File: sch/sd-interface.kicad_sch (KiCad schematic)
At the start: 33 parts, among them J15 F32Q-1A7H1-11022, J16 MEM2075-00-140-01-A, J17 5V_out, J19 3V3_in, Q1 Q_PMOS_GSD, U10 CD4043BDR, U11 TPS22919DCKR, U8 MAX4996LETG_

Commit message: started pcb design
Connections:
- net R_En_switch: now also U10.3 (R1)
- net S_En_switch: now also U10.4 (S1)
- net at TP19.1, U10.10 (Q3), U8.15 (EN): no longer R15.2, R16.1
- net at U10.2 (Q1): now also R15.2, R16.1
- no-connect marks 7 -> 4
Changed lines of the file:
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@@
+	)
+	(junction
+		(at 302.26 132.08)
+		(diameter 0)
+		(color 0 0 0 0)
 	)
 	(junction
@@
 	)
 	(junction
-		(at 204.47 144.78)
+		(at 302.26 142.24)
 		(diameter 0)
 		(color 0 0 0 0)
@@
 	)
 	(no_connect
-		(at 299.72 147.32)
-	)
-	(no_connect
 		(at 299.72 125.73)
 	)
@@
 	)
 	(no_connect
-		(at 299.72 137.16)
-	)
-	(no_connect
 		(at 279.4 227.33)
 	)
@@
 		(at 175.26 266.7)
 	)
-	(no_connect
-		(at 264.16 149.86)
-	)
 	(wire
 		(pts
@@
 	(wire
 		(pts
+			(xy 299.72 137.16) (xy 302.26 137.16)
+		)
+		(stroke
+			(width 0)
+			(type default)
+		)
+	)
+	(wire
+		(pts
 			(xy 152.4 66.04) (xy 152.4 69.85)
 		)
@@
 	(wire
 		(pts
-			(xy 204.47 151.13) (xy 204.47 144.78)
-		)
-		(stroke
-			(width 0)
-			(type default)
-		)
-	)
-	(wire
-		(pts
 			(xy 234.95 73.66) (xy 234.95 62.23)
 		)
@@
 	(wire
 		(pts
+			(xy 302.26 132.08) (xy 335.28 132.08)
+		)
+		(stroke
+			(width 0)
+			(type default)
+		)
+	)
+	(wire
+		(pts
 			(xy 99.06 163.83) (xy 99.06 190.5)
 		)
@@
 	(wire
 		(pts
-			(xy 299.72 142.24) (xy 335.28 142.24)
+			(xy 299.72 142.24) (xy 302.26 142.24)
 		)
 		(stroke
@@
 	(wire
 		(pts
+			(xy 215.9 149.86) (xy 215.9 229.87)
+		)
+		(stroke
+			(width 0)
+			(type default)
+		)
+	)
+	(wire
+		(pts
 			(xy 71.12 87.63) (xy 71.12 123.19)
 		)
@@
 	(wire
 		(pts
-			(xy 215.9 151.13) (xy 204.47 151.13)
-		)
-		(stroke
-			(width 0)
-			(type default)
-		)
-	)
-	(wire
-		(pts
 			(xy 346.71 218.44) (xy 346.71 220.98)
 		)
@@
 	(wire
 		(pts
-			(xy 215.9 229.87) (xy 215.9 151.13)
-		)
-		(stroke
-			(width 0)
-			(type default)
-		)
-	)
-	(wire
-		(pts
 			(xy 111.76 36.83) (xy 111.76 50.8)
 		)
@@
 	(wire
 		(pts
+			(xy 302.26 142.24) (xy 335.28 142.24)
+		)
+		(stroke
+			(width 0)
+			(type default)
+		)
+	)
+	(wire
+		(pts
+			(xy 264.16 149.86) (xy 215.9 149.86)
+		)
+		(stroke
+			(width 0)
+			(type default)
+		)
+	)
+	(wire
+		(pts
 			(xy 207.01 62.23) (xy 234.95 62.23)
 		)
@@
 	(wire
 		(pts
+			(xy 302.26 142.24) (xy 302.26 147.32)
+		)
+		(stroke
+			(width 0)
+			(type default)
+		)
+	)
+	(wire
+		(pts
 			(xy 96.52 36.83) (xy 99.06 36.83)
 		)
@@
 	(wire
 		(pts
-			(xy 299.72 132.08) (xy 335.28 132.08)
+			(xy 299.72 132.08) (xy 302.26 132.08)
 		)
 		(stroke
@@
 	(wire
 		(pts
+			(xy 302.26 137.16) (xy 302.26 132.08)
+		)
+		(stroke
+			(width 0)
+			(type default)
+		)
+	)
+	(wire
+		(pts
 			(xy 130.81 203.2) (xy 173.99 203.2)
 		)
@@
 		)
 		(stroke
+			(width 0)
+			(type default)
+		)
+	)
+	(wire
+		(pts
+			(xy 302.26 147.32) (xy 299.72 147.32)
+		)
+		(stroke

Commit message: work pcb about 70 percent
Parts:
- TP10, TP11, TP12, TP7, TP8, TP9: footprint TestPoint:TestPoint_Loop_D2.50mm_Drill1.85mm -> TestPoint:TestPoint_Pad_D1.0mm
- TP13, TP14, TP15, TP16, TP17, TP18, TP19: footprint TestPoint:TestPoint_Loop_D2.50mm_Drill1.85mm -> TestPoint:TestPoint_Loop_D2.60mm_Drill1.6mm_Beaded
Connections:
- net +3V3_e is gone; now on net +3V3: C20.1, C9.1, J19.1, Q1.2 (S), R15.1, U8.14 (VCC)
- net +3v3_e is gone; now on net +3V3: C13.1, U10.16 (VDD), U10.5 (EN)
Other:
- note removed: "CIRCUIT IS DESIGNED FOR ONLY 3.3V SD OPERATION, NOT 1.8V"
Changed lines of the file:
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@@
 		)
 	)
-	(text "CIRCUIT IS DESIGNED FOR ONLY 3.3V SD \nOPERATION, NOT 1.8V"
-		(exclude_from_sim no)
-		(at 304.8 29.718 0)
-		(effects
-			(font
-				(size 1.27 1.27)
-			)
-		)
-	)
 	(text "8: DAT1 // X"
 		(exclude_from_sim no)
@@
 		)
 	)
-	(global_label "+3V3_e"
+	(global_label "+3V3"
 		(shape input)
 		(at 146.05 153.67 0)
@@
 		)
 		(property "Intersheetrefs" "${INTERSHEET_REFS}"
-			(at 156.1714 153.67 0)
+			(at 154.1152 153.67 0)
 			(effects
 				(font
@@
 		)
 	)
-	(global_label "+3V3_e"
+	(global_label "+3V3"
 		(shape input)
 		(at 194.31 222.25 180)
@@
 		)
 	)
-	(global_label "+3v3_e"
+	(global_label "+3V3"
 		(shape input)
 		(at 252.73 154.94 180)
@@
 		)
 		(property "Intersheetrefs" "${INTERSHEET_REFS}"
-			(at 246.3582 154.94 0)
+			(at 244.6648 154.94 0)
 			(effects
 				(font
@@
 		)
 	)
-	(global_label "+3V3_e"
+	(global_label "+3V3"
 		(shape output)
 		(at 313.69 48.26 180)
@@
 		)
 		(property "Intersheetrefs" "${INTERSHEET_REFS}"
-			(at 303.5686 48.26 0)
+			(at 305.6248 48.26 0)
 			(effects
 				(font
@@
 			)
 		)
-		(property "Footprint" "TestPoint:TestPoint_Loop_D2.50mm_Drill1.85mm"
+		(property "Footprint" "TestPoint:TestPoint_Loop_D2.60mm_Drill1.6mm_Beaded"
 			(at 213.36 73.66 0)
 			(effects
@@
 			)
 		)
-		(property "Footprint" "TestPoint:TestPoint_Loop_D2.50mm_Drill1.85mm"
+		(property "Footprint" "TestPoint:TestPoint_Loop_D2.60mm_Drill1.6mm_Beaded"
 			(at 200.66 261.62 0)
 			(effects
@@
 			)
 		)
-		(property "Footprint" "TestPoint:TestPoint_Loop_D2.50mm_Drill1.85mm"
+		(property "Footprint" "TestPoint:TestPoint_Pad_D1.0mm"
 			(at 76.2 158.75 0)
 			(effects
@@
 			)
 		)
-		(property "Footprint" "TestPoint:TestPoint_Loop_D2.50mm_Drill1.85mm"
+		(property "Footprint" "TestPoint:TestPoint_Loop_D2.60mm_Drill1.6mm_Beaded"
 			(at 222.25 73.66 0)
 			(effects
@@
 			)
 		)
-		(property "Footprint" "TestPoint:TestPoint_Loop_D2.50mm_Drill1.85mm"
+		(property "Footprint" "TestPoint:TestPoint_Loop_D2.60mm_Drill1.6mm_Beaded"
 			(at 252.73 138.43 0)
 			(effects
@@
 			)
 		)
-		(property "Footprint" "TestPoint:TestPoint_Loop_D2.50mm_Drill1.85mm"
+		(property "Footprint" "TestPoint:TestPoint_Pad_D1.0mm"
 			(at 91.44 158.75 0)
 			(effects
@@
 			)
 		)
-		(property "Footprint" "TestPoint:TestPoint_Loop_D2.50mm_Drill1.85mm"
+		(property "Footprint" "TestPoint:TestPoint_Loop_D2.60mm_Drill1.6mm_Beaded"
 			(at 229.87 73.66 0)
 			(effects
@@
 			)
 		)
-		(property "Footprint" "TestPoint:TestPoint_Loop_D2.50mm_Drill1.85mm"
+		(property "Footprint" "TestPoint:TestPoint_Loop_D2.60mm_Drill1.6mm_Beaded"
 			(at 240.03 138.43 0)
 			(effects
@@
 			)
 		)
-		(property "Footprint" "TestPoint:TestPoint_Loop_D2.50mm_Drill1.85mm"
+		(property "Footprint" "TestPoint:TestPoint_Pad_D1.0mm"
 			(at 114.3 158.75 0)
 			(effects
@@
 			)
 		)
-		(property "Footprint" "TestPoint:TestPoint_Loop_D2.50mm_Drill1.85mm"
+		(property "Footprint" "TestPoint:TestPoint_Loop_D2.60mm_Drill1.6mm_Beaded"
 			(at 237.49 73.66 0)
 			(effects
@@
 			)
 		)
-		(property "Footprint" "TestPoint:TestPoint_Loop_D2.50mm_Drill1.85mm"
+		(property "Footprint" "TestPoint:TestPoint_Pad_D1.0mm"
 			(at 121.92 158.75 0)
 			(effects
@@
 			)
 		)
-		(property "Footprint" "TestPoint:TestPoint_Loop_D2.50mm_Drill1.85mm"
+		(property "Footprint" "TestPoint:TestPoint_Pad_D1.0mm"
 			(at 68.58 158.75 0)
 			(effects
@@
 			)
 		)
-		(property "Footprint" "TestPoint:TestPoint_Loop_D2.50mm_Drill1.85mm"
+		(property "Footprint" "TestPoint:TestPoint_Pad_D1.0mm"
 			(at 99.06 158.75 0)
 			(effects

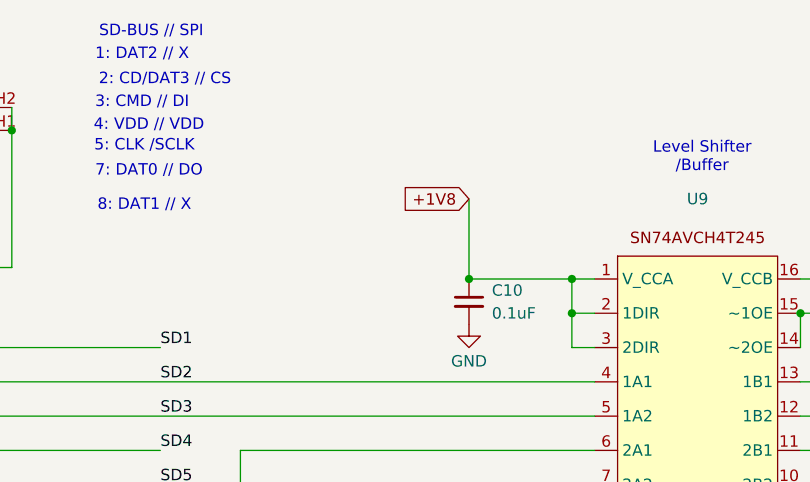
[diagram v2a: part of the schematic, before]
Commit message: partially route the powerlines
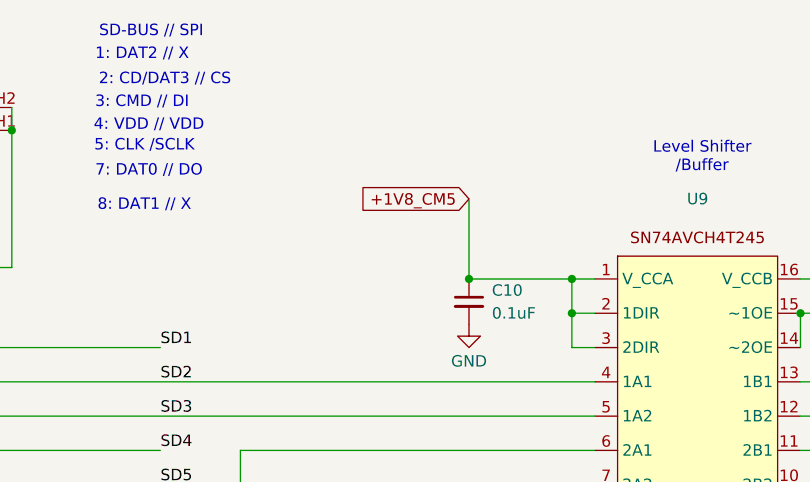
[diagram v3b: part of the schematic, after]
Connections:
- net +1V8 renamed +1V8_CM5
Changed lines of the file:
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@@
 		)
 	)
-	(global_label "+1V8"
+	(global_label "+1V8_CM5"
 		(shape input)
 		(at 170.18 34.29 180)

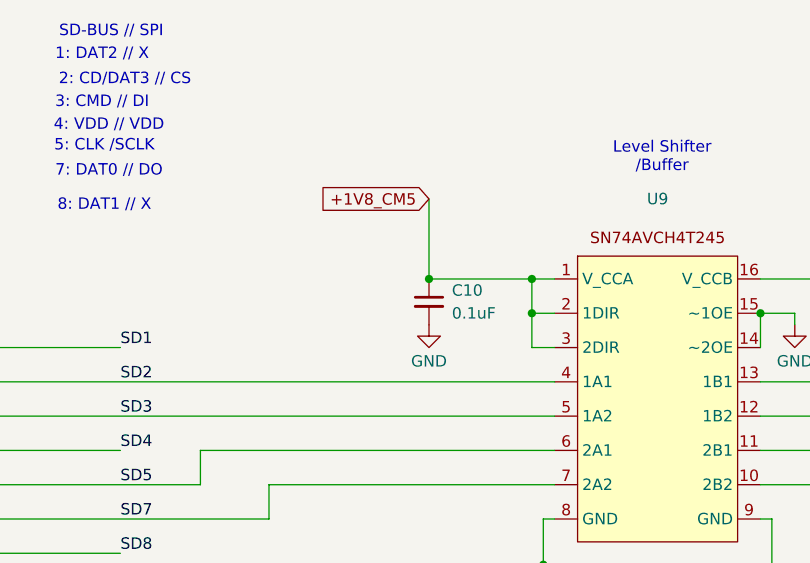
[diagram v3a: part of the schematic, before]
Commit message: powergrid complete, still missing antennas
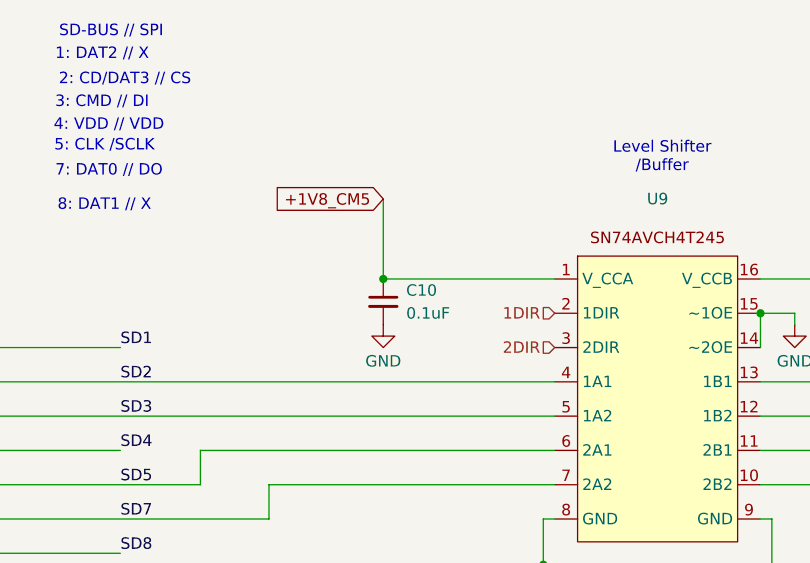
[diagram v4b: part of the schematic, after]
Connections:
- net +1V8_CM5: no longer U9.2 (1DIR), U9.3 (2DIR)
- new net 1DIR: U9.2 (1DIR)
- new net 2DIR: U9.3 (2DIR)
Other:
- moved on the sheet: C10
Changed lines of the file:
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@@
 	)
 	(junction
-		(at 181.61 43.18)
-		(diameter 0)
-		(color 0 0 0 0)
-	)
-	(junction
 		(at 326.39 48.26)
 		(diameter 0)
@@
 	)
 	(junction
-		(at 181.61 46.99)
-		(diameter 0)
-		(color 0 0 0 0)
-	)
-	(junction
 		(at 135.89 182.88)
 		(diameter 0)
@@
 	)
 	(junction
-		(at 170.18 43.18)
+		(at 165.1 43.18)
 		(diameter 0)
 		(color 0 0 0 0)
@@
 	(wire
 		(pts
-			(xy 181.61 46.99) (xy 181.61 43.18)
-		)
-		(stroke
-			(width 0)
-			(type default)
-		)
-	)
-	(wire
-		(pts
 			(xy 60.96 123.19) (xy 60.96 114.3)
 		)
@@
 	(wire
 		(pts
-			(xy 184.15 50.8) (xy 181.61 50.8)
-		)
-		(stroke
-			(width 0)
-			(type default)
-		)
-	)
-	(wire
-		(pts
 			(xy 208.28 69.85) (xy 208.28 74.93)
 		)
@@
 	(wire
 		(pts
-			(xy 170.18 34.29) (xy 170.18 43.18)
+			(xy 165.1 34.29) (xy 165.1 43.18)
 		)
 		(stroke
@@
 	(wire
 		(pts
-			(xy 181.61 46.99) (xy 184.15 46.99)
-		)
-		(stroke
-			(width 0)
-			(type default)
-		)
-	)
-	(wire
-		(pts
 			(xy 124.46 123.19) (xy 124.46 107.95)
 		)
@@
 	(wire
 		(pts
-			(xy 181.61 50.8) (xy 181.61 46.99)
-		)
-		(stroke
-			(width 0)
-			(type default)
-		)
-	)
-	(wire
-		(pts
 			(xy 208.28 74.93) (xy 182.88 74.93)
 		)
@@
 	(wire
 		(pts
-			(xy 170.18 43.18) (xy 181.61 43.18)
-		)
-		(stroke
-			(width 0)
-			(type default)
-		)
-	)
-	(wire
-		(pts
-			(xy 181.61 43.18) (xy 184.15 43.18)
+			(xy 165.1 43.18) (xy 184.15 43.18)
 		)
 		(stroke
@@
 	(global_label "+1V8_CM5"
 		(shape input)
-		(at 170.18 34.29 180)
+		(at 165.1 34.29 180)
 		(fields_autoplaced yes)
 		(effects
@@
 		)
 		(property "Intersheetrefs" "${INTERSHEET_REFS}"
-			(at 162.1148 34.29 0)
+			(at 157.0348 34.29 0)
 			(effects
 				(font
@@
 		)
 	)
+	(hierarchical_label "1DIR"
+		(shape input)
+		(at 184.15 46.99 180)
+		(effects
+			(font
+				(size 1.27 1.27)
+			)
+			(justify right)
+		)
+	)
 	(hierarchical_label "R_En_switch"
 		(shape input)
@@
 		)
 	)
+	(hierarchical_label "2DIR"
+		(shape input)
+		(at 184.15 50.8 180)
+		(effects
+			(font
+				(size 1.27 1.27)
+			)
+			(justify right)
+		)
+	)
 	(symbol
 		(lib_id "691137710002:691137710002")
@@
 	(symbol
 		(lib_id "Device:C_Small")
-		(at 170.18 45.72 0)
+		(at 165.1 45.72 0)
 		(unit 1)
 		(exclude_from_sim no)
@@
 		(fields_autoplaced yes)
 		(property "Reference" "C10"
-			(at 172.72 44.4562 0)
+			(at 167.64 44.4562 0)
 			(effects
 				(font
@@
 		)
 		(property "Value" "0.1uF"
-			(at 172.72 46.9962 0)
+			(at 167.64 46.9962 0)
 			(effects
 				(font
@@
 		)
 		(property "Footprint" "Capacitor_SMD:C_0603_1608Metric"
-			(at 170.18 45.72 0)
+			(at 165.1 45.72 0)
 			(effects
 				(font
@@
 		)
 		(property "Datasheet" "~"
-			(at 170.18 45.72 0)
+			(at 165.1 45.72 0)
 			(effects
 				(font
@@
 		)
 		(property "Description" "Unpolarized capacitor, small symbol"
-			(at 170.18 45.72 0)
+			(at 165.1 45.72 0)
 			(effects
 				(font
@@
 		)
 		(property "MPN" "C0603C104K3RACTU"
-			(at 170.18 45.72 0)
+			(at 165.1 45.72 0)
 			(effects
 				(font
@@
 	(symbol
 		(lib_id "power:GND")
-		(at 170.18 48.26 0)
+		(at 165.1 48.26 0)
 		(unit 1)
 		(exclude_from_sim no)
@@
 		(dnp no)
 		(property "Reference" "#PWR045"
-			(at 170.18 54.61 0)
+			(at 165.1 54.61 0)
 			(effects
 				(font
@@
 		)
 		(property "Value" "GND"
-			(at 170.18 52.324 0)
+			(at 165.1 52.324 0)
 			(effects
 				(font
@@
 		)
 		(property "Footprint" ""
-			(at 170.18 48.26 0)
+			(at 165.1 48.26 0)
 			(effects
 				(font
@@
 		)
 		(property "Datasheet" ""
-			(at 170.18 48.26 0)
+			(at 165.1 48.26 0)
 			(effects
 				(font
@@
 		)
 		(property "Description" "Power symbol creates a global label with name \"GND\" , ground"
-			(at 170.18 48.26 0)
+			(at 165.1 48.26 0)
 			(effects
 				(font

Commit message: earth plane, vias, connector ect
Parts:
- added TP20, TP21: TestPoint, TestPoint:TestPoint_Pad_D1.0mm, symbol Connector:TestPoint
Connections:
- net Buffer_sd3: now also TP20.1
- net Buffer_sd5: now also TP21.1
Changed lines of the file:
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@@
 	)
 	(junction
+		(at 255.27 58.42)
+		(diameter 0)
+		(color 0 0 0 0)
+	)
+	(junction
 		(at 182.88 74.93)
 		(diameter 0)
@@
 	)
 	(junction
+		(at 264.16 62.23)
+		(diameter 0)
+		(color 0 0 0 0)
+	)
+	(junction
 		(at 91.44 163.83)
 		(diameter 0)
@@
 	(wire
 		(pts
-			(xy 227.33 58.42) (xy 274.32 58.42)
+			(xy 227.33 58.42) (xy 255.27 58.42)
 		)
 		(stroke
@@
 	(wire
 		(pts
+			(xy 255.27 58.42) (xy 255.27 69.85)
+		)
+		(stroke
+			(width 0)
+			(type default)
+		)
+	)
+	(wire
+		(pts
 			(xy 50.8 41.91) (xy 50.8 68.58)
 		)
@@
 	(wire
 		(pts
+			(xy 264.16 62.23) (xy 274.32 62.23)
+		)
+		(stroke
+			(width 0)
+			(type default)
+		)
+	)
+	(wire
+		(pts
 			(xy 170.18 232.41) (xy 172.72 232.41)
 		)
@@
 	(wire
 		(pts
+			(xy 255.27 58.42) (xy 274.32 58.42)
+		)
+		(stroke
+			(width 0)
+			(type default)
+		)
+	)
+	(wire
+		(pts
 			(xy 144.78 62.23) (xy 144.78 66.04)
 		)
@@
 	(wire
 		(pts
-			(xy 234.95 62.23) (xy 274.32 62.23)
+			(xy 234.95 62.23) (xy 264.16 62.23)
 		)
 		(stroke
@@
 	(wire
 		(pts
+			(xy 264.16 62.23) (xy 264.16 69.85)
+		)
+		(stroke
+			(width 0)
+			(type default)
+		)
+	)
+	(wire
+		(pts
 			(xy 86.36 36.83) (xy 86.36 41.91)
 		)
@@
 	)
 	(symbol
+		(lib_id "Connector:TestPoint")
+		(at 264.16 69.85 180)
+		(unit 1)
+		(exclude_from_sim no)
+		(in_bom yes)
+		(on_board yes)
+		(dnp no)
+		(fields_autoplaced yes)
+		(property "Reference" "TP21"
+			(at 266.7 73.1519 0)
+			(effects
+				(font
+					(size 1.27 1.27)
+				)
+				(justify right)
+			)
+		)
+		(property "Value" "TestPoint"
+			(at 261.62 71.8821 0)
+			(effects
+				(font
+					(size 1.27 1.27)
+				)
+				(justify left)
+				(hide yes)
+			)
+		)
+		(property "Footprint" "TestPoint:TestPoint_Pad_D1.0mm"
+			(at 259.08 69.85 0)
+			(effects
+				(font
+					(size 1.27 1.27)
+				)
+				(hide yes)
+			)
+		)
+		(property "Datasheet" "~"
+			(at 259.08 69.85 0)
+			(effects
+				(font
+					(size 1.27 1.27)
+				)
+				(hide yes)
+			)
+		)
+		(property "Description" "test point"
+			(at 264.16 69.85 0)
+			(effects
+				(font
+					(size 1.27 1.27)
+				)
+				(hide yes)
+			)
+		)
+		(pin "1"
+		)
+		(instances
+			(project "audiograb"
+				(path "/c46c2311-6d4b-411d-b012-c7730eac136d/6c55ccce-577d-49c2-8294-3a5d8e11981e"
+					(reference "TP21")
+					(unit 1)
+				)
+			)
+		)
+	)
+	(symbol
 		(lib_id "power:GND")
 		(at 346.71 220.98 0)
@@
 					(unit 1)
 				)
+			)
+		)
+	)
+	(symbol
+		(lib_id "Connector:TestPoint")
+		(at 255.27 69.85 180)
+		(unit 1)
+		(exclude_from_sim no)
+		(in_bom yes)
+		(on_board yes)
+		(dnp no)
+		(fields_autoplaced yes)
+		(property "Reference" "TP20"
+			(at 257.81 73.1519 0)
+			(effects
+				(font
+					(size 1.27 1.27)
+				)
+				(justify right)
+			)
+		)
+		(property "Value" "TestPoint"
+			(at 252.73 71.8821 0)
+			(effects
+				(font
+					(size 1.27 1.27)
+				)
+				(justify left)
+				(hide yes)
+			)
+		)
+		(property "Footprint" "TestPoint:TestPoint_Pad_D1.0mm"
+			(at 250.19 69.85 0)
+			(effects
+				(font
+					(size 1.27 1.27)
+				)
+				(hide yes)
+			)
+		)
+		(property "Datasheet" "~"
+			(at 250.19 69.85 0)
+			(effects
+				(font
+					(size 1.27 1.27)
+				)
+				(hide yes)
+			)
+		)
+		(property "Description" "test point"
+			(at 255.27 69.85 0)
+			(effects
+				(font
+					(size 1.27 1.27)
+				)
+				(hide yes)
+			)
+		)
+		(pin "1"
+		)
+		(instances
+			(project "audiograb"
+				(path "/c46c2311-6d4b-411d-b012-c7730eac136d/6c55ccce-577d-49c2-8294-3a5d8e11981e"
+					(reference "TP20")
+					(unit 1)
+				)

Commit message: pågebynt merging av pwr-supply og modem branches
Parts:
- removed C20: 100n, Capacitor_SMD:C_0603_1608Metric, symbol Device:C
- removed J19: 3V3_in, 691137710002:691137710002, symbol 691137710002:691137710002
- added R3: 47k, Resistor_SMD:R_0603_1608Metric, symbol Device:R
- renumbered C13 to C10, C14 to C11, C9 to C6, C10 to C7, C11 to C8, C12 to C9, CR1 to CR2, CR2 to CR3, J15 to J5, J16 to J6, J17 to J8, R15 to R4, R16 to R5, TP7 to TP1, TP16 to TP10, TP17 to TP11, TP18 to TP12, TP19 to TP13, TP20 to TP14, TP21 to TP15, TP8 to TP2, TP9 to TP3, TP10 to TP4, TP11 to TP5, TP12 to TP6, TP13 to TP7, TP14 to TP8, TP15 to TP9, U8 to U2, U9 to U3, U10 to U4, U11 to U5
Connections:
- net 2DIR is gone; now on an unnamed net: U3.3 (2DIR)
- net +1V8_CM5: now also R3.1
- net +3V3 renamed +3V3_CM5
- net 1DIR: no longer names the net of U3.2 (1DIR)
- net 1DIR: now also R3.2
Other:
- note added: "Testpoints at CM"
- note added: "Testpoints at buffer"
- moved on the sheet: TP10, TP12, TP8, TP9
